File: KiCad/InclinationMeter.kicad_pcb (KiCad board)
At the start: 4 copper layers, 90 x 70 mm, 115 parts, among them J1 JST_PH_2.0mm_1x02, J2 USB-C, J3 Header_FFC_1.0mm_06, J4 Header_50mil_2x07, J5 Header_FFC_1.0mm_10, J6 Header_FFC_1.0mm_10, Q1 DMG2305UX, Q2 FS8205A, Q3 DMG2305UX, Q4 AO3400A, Q5 AO3400A, SW1 PEC11R-4215F-S0024, SW2 PEC11R-4215F-S0024, U1 DW01A, U10 SN74HC14PWR, U11 LM35DGS, U12 BME280, U2 LP5907MFX-3.3/NOPB, U3 TP4056, U4 LP5907MFX-3.3/NOPB, U5 SD6210A, U6 STM32G0B1RET6, U7 RN4871-I_RM128, U8 SN74AHCT244DBR, U9 24LC256-I_ST, Y1 32.768kHz, Y2 8MHz

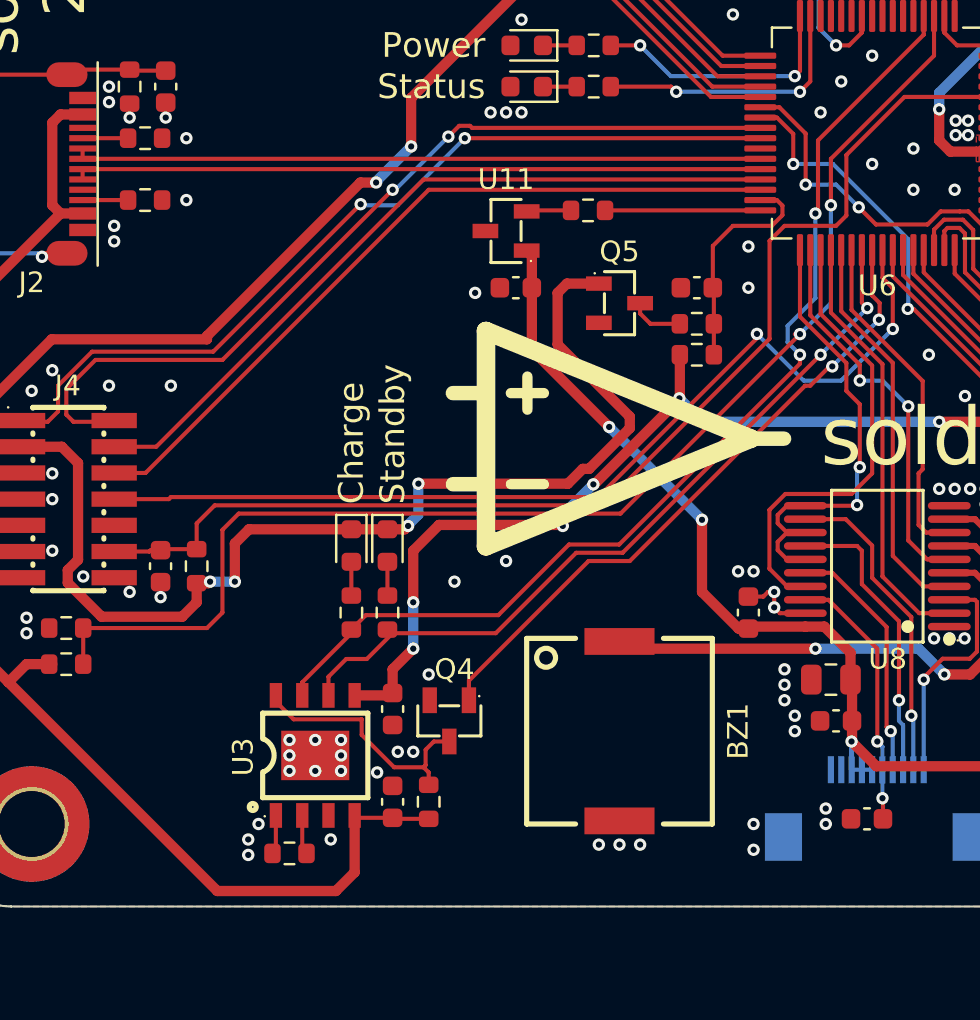
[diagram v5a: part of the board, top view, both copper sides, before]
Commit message: External temperature sensor added
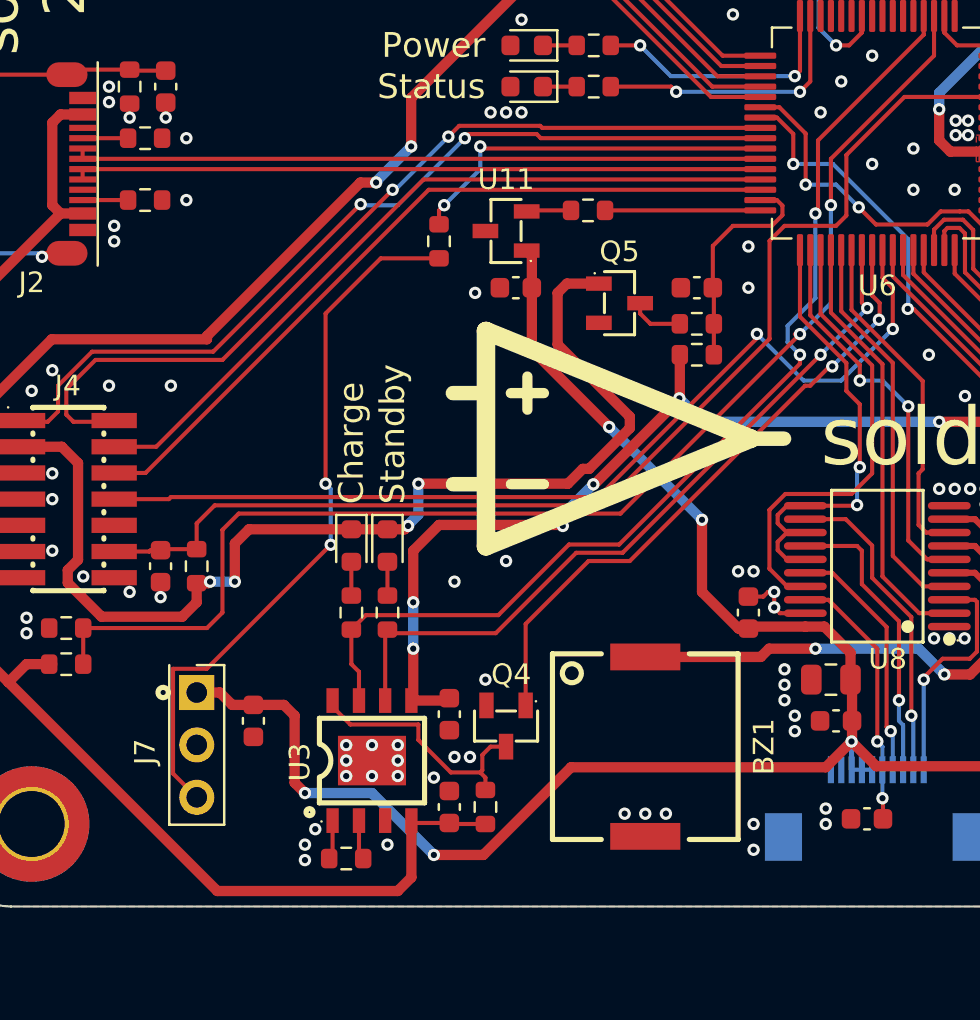
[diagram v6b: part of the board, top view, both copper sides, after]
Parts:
- added C43: 100n, sldrnrd:C_0603, F.Cu at (64.8, 91.0)
- added J7: Header_100mil_1x03, sldrnrd:Header_100mil_1x03, F.Cu at (62.0, 89.6)
- added R37: 2k, sldrnrd:R_0603, F.Cu at (73.8, 67.8)
- moved C5 2.76 mm to (74.2, 95.2)
- moved C7 2.76 mm to (74.2, 90.7)
- moved Q4 2.76 mm to (77.0, 91.2)
- moved R4 2.76 mm to (69.2, 97.7)
- moved R5 2.76 mm to (76.0, 95.2)
- moved U3 2.76 mm to (70.5, 92.9)
- moved BZ1 1.46 mm to (83.8, 92.2)
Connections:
- U6 pad 42: unconnected-(U6-PA10-Pad42) -> TEMP_SENSE_EXT
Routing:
- net 5V0: track 50.8 -> 90.0 mm, vias 3 -> 5
- net Net-(J7-Pad3): track 0.00 -> 34.8 mm, vias 0 -> 2
- net TEMP_SENSE_EXT: track 0.00 -> 18.2 mm, vias 0 -> 2
- net V_USB: track 62.9 -> 65.5 mm
- net STANDBY_SENSE: track 37.4 -> 35.9 mm
- net BUZZER_5V: track 31.1 -> 29.8 mm
- net ~{CHARGE_EN}: track 31.6 -> 30.7 mm
